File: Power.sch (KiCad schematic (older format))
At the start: 35 parts, among them T5 Test_Point, T6 Test_Point, T7 Test_Point, U4 MP4570GF, U5 AP65251, U6 AZ1117-3.3

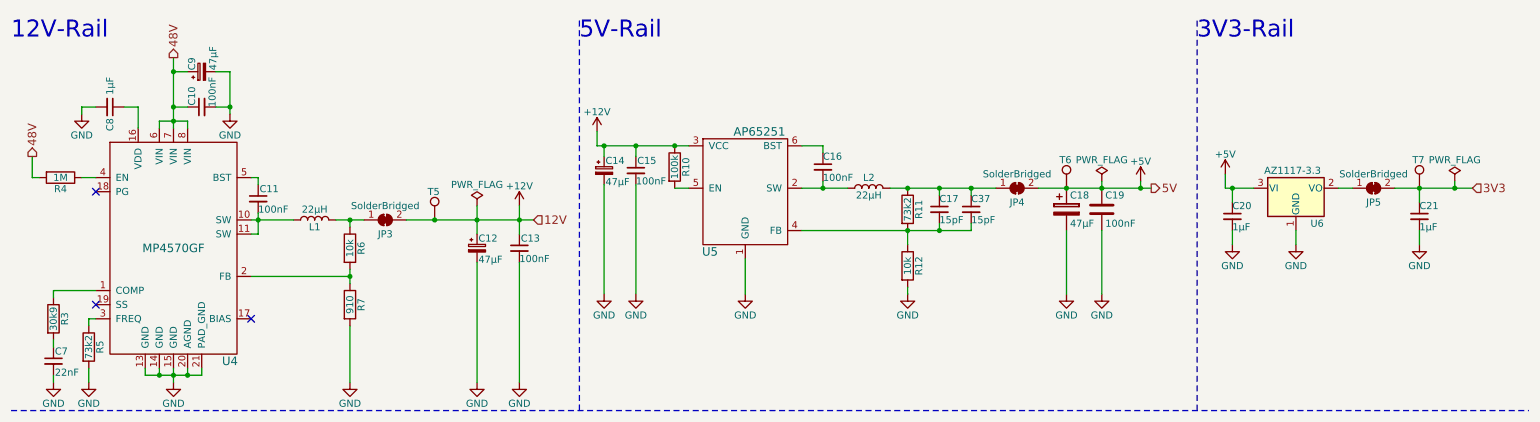
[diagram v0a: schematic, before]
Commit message: Filled in the Parts for the Fault-Indicator
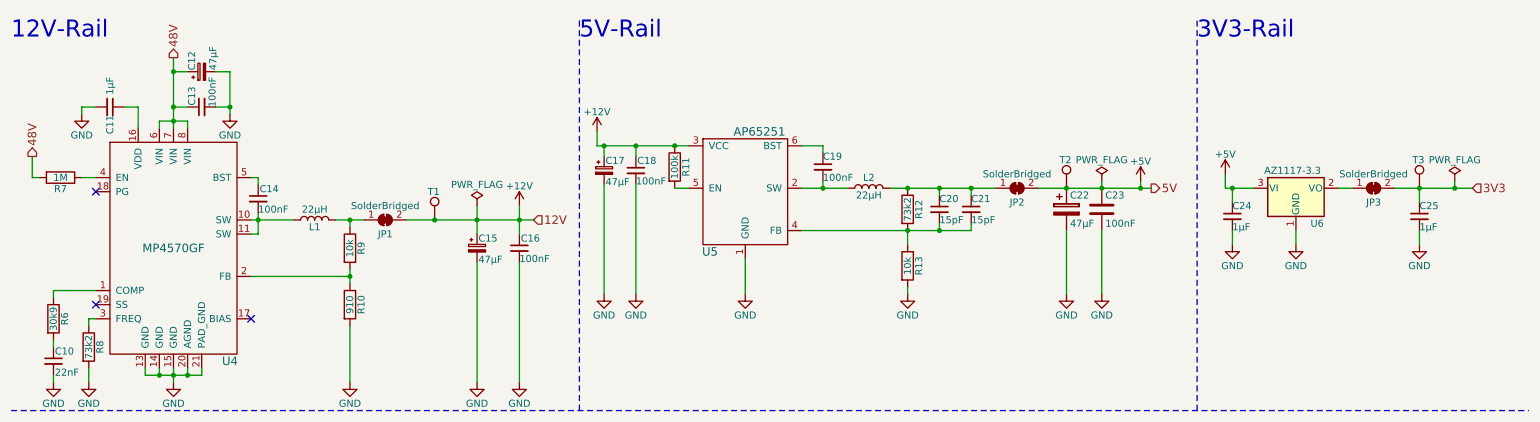
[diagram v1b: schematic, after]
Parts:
- renumbered C7 to C10, C8 to C11, C9 to C12, C10 to C13, C11 to C14, C12 to C15, C13 to C16, C14 to C17, C15 to C18, C16 to C19, C17 to C20, C37 to C21, C18 to C22, C19 to C23, C20 to C24, C21 to C25, JP3 to JP1, JP4 to JP2, JP5 to JP3, R7 to R10, R10 to R11, R11 to R12, R12 to R13, R3 to R6, R4 to R7, R5 to R8, R6 to R9, T5 to T1, T6 to T2, T7 to T3

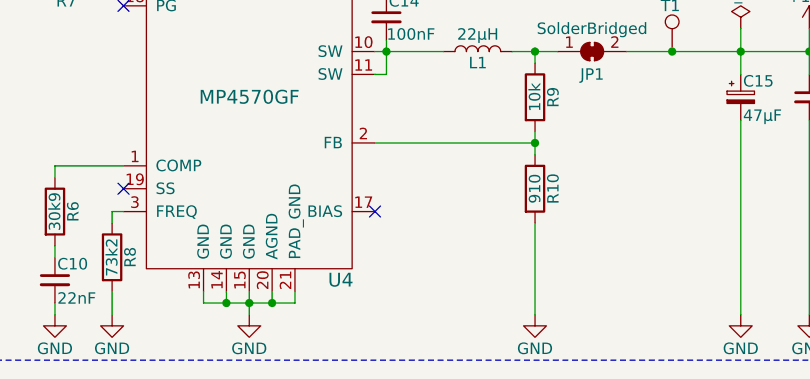
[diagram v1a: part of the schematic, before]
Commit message: Added missing bias-cap
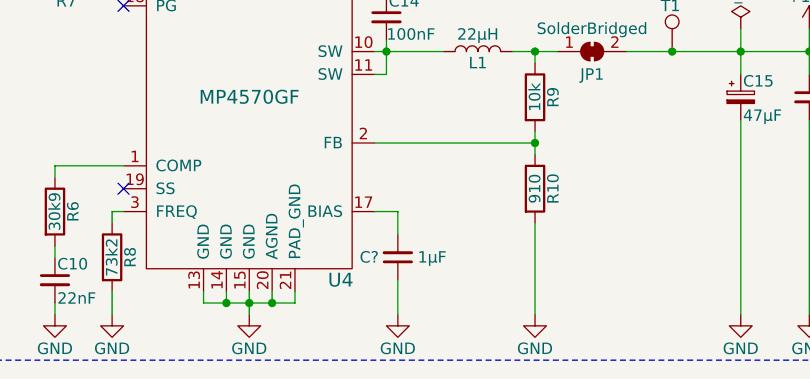
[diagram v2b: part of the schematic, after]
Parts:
- added C?: 1μF, Capacitor_SMD:C_0805_2012Metric, symbol Device:C_Small
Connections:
- net GND: now also C?.1
- net at U4.17 (BIAS): now also C?.2
- no-connect marks 3 -> 2
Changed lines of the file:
@@
 	1925 1100 2025 1100
 Connection ~ 2025 1100
-NoConn ~ 2175 2600
 $Comp
 L Device:R R9
@@
 Wire Wire Line
 	10450 1975 10450 2075
+$Comp
+L Device:C_Small C?
+U 1 1 5B7479D3
+P 2275 2800
+F 0 "C?" H 2400 2800 50  0000 C CNN
+F 1 "1μF" H 2125 2800 50  0000 C CNN
+F 2 "Capacitor_SMD:C_0805_2012Metric" H 2275 2800 50  0001 C CNN
+F 3 "~" H 2275 2800 50  0001 C CNN
+F 4 "https://www.digikey.com/product-detail/en/taiyo-yuden/TMK212B7105MG-T/587-5595-1-ND/7067270" H 2275 2800 50  0001 C CNN "Buy"
+	1    2275 2800
+	-1   0    0    1
+$EndComp
+Wire Wire Line
+	2175 2600 2275 2600
+Wire Wire Line
+	2275 2600 2275 2700
+$Comp
+L power:GND #PWR?
+U 1 1 5B74AE60
+P 2275 3050
+F 0 "#PWR?" H 2275 2800 50  0001 C CNN
+F 1 "GND" H 2275 2900 50  0000 C CNN
+F 2 "" H 2275 3050 50  0001 C CNN
+F 3 "" H 2275 3050 50  0001 C CNN
+	1    2275 3050
+	1    0    0    -1
+$EndComp
+Wire Wire Line
+	2275 2900 2275 3050
 $EndSCHEMATC

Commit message: Migrated connectors to new libraries
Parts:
- T1, T2, T3: symbol Connector_Specialized:Test_Point -> Connector:TestPoint
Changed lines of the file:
@@
 $EndComp
 $Comp
-L Connector_Specialized:Test_Point T3
+L Connector:TestPoint T3
 U 1 1 5AB61A04
 P 10450 1675
@@
 Connection ~ 10450 1675
 $Comp
-L Connector_Specialized:Test_Point T2
+L Connector:TestPoint T2
 U 1 1 5AB7C501
 P 7950 1675
@@
 Connection ~ 7950 1675
 $Comp
-L Connector_Specialized:Test_Point T1
+L Connector:TestPoint T1
 U 1 1 5AB8F83C
 P 3475 1900

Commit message: Replaced OOS-Parts
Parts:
- C11, C24, C25, C?: Buy https://www.digikey.com/product-detail/en/taiyo-yuden/TMK21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 -> https://www.digikey.com/short/jw2293
- R10: Buy https://www.digikey.com/product-detail/en/yageo/RC0603FR-07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 -> https://www.digikey.com/short/jw22zf
- R8: Buy https://www.digikey.com/product-detail/en/yageo/RC0603FR-07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 -> https://www.digikey.com/short/jw22qc
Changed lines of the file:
@@
 F 2 "Resistor_SMD:R_0603_1608Metric" V 955 2800 50  0001 C CNN
 F 3 "" H 1025 2800 50  0001 C CNN
-F 4 "https://www.digikey.com/product-detail/en/yageo/RC0603FR-0773K2L/311-73.2KHRCT-ND/730321" V 1025 2800 50  0001 C CNN "Buy"
+F 4 "https://www.digikey.com/short/jw22qc" V 1025 2800 50  0001 C CNN "Buy"
 	1    1025 2800
 	1    0    0    -1
@@
 F 2 "Resistor_SMD:R_0603_1608Metric" V 2805 2500 50  0001 C CNN
 F 3 "" H 2875 2500 50  0001 C CNN
-F 4 "https://www.digikey.com/product-detail/en/yageo/RC0603FR-07909RL/311-909HRCT-ND/730372" V 2875 2500 50  0001 C CNN "Buy"
+F 4 "https://www.digikey.com/short/jw22zf" V 2875 2500 50  0001 C CNN "Buy"
 	1    2875 2500
 	1    0    0    -1
@@
 F 2 "Capacitor_SMD:C_0805_2012Metric" H 1175 1100 50  0001 C CNN
 F 3 "~" H 1175 1100 50  0001 C CNN
-F 4 "https://www.digikey.com/product-detail/en/taiyo-yuden/TMK212B7105MG-T/587-5595-1-ND/7067270" H 1175 1100 50  0001 C CNN "Buy"
+F 4 "https://www.digikey.com/short/jw2293" H 1175 1100 50  0001 C CNN "Buy"
 	1    1175 1100
 	0    1    1    0
@@
 F 2 "Capacitor_SMD:C_0805_2012Metric" H 9163 1725 50  0001 C CNN
 F 3 "~" H 9125 1875 50  0001 C CNN
-F 4 "https://www.digikey.com/product-detail/en/taiyo-yuden/TMK212B7105MG-T/587-5595-1-ND/7067270" H 9125 1875 50  0001 C CNN "Buy"
+F 4 "https://www.digikey.com/short/jw2293" H 9125 1875 50  0001 C CNN "Buy"
 	1    9125 1875
 	1    0    0    -1
@@
 F 2 "Capacitor_SMD:C_0805_2012Metric" H 10488 1725 50  0001 C CNN
 F 3 "~" H 10450 1875 50  0001 C CNN
-F 4 "https://www.digikey.com/product-detail/en/taiyo-yuden/TMK212B7105MG-T/587-5595-1-ND/7067270" H 10450 1875 50  0001 C CNN "Buy"
+F 4 "https://www.digikey.com/short/jw2293" H 10450 1875 50  0001 C CNN "Buy"
 	1    10450 1875
 	1    0    0    -1
@@
 F 2 "Capacitor_SMD:C_0805_2012Metric" H 2275 2800 50  0001 C CNN
 F 3 "~" H 2275 2800 50  0001 C CNN
-F 4 "https://www.digikey.com/product-detail/en/taiyo-yuden/TMK212B7105MG-T/587-5595-1-ND/7067270" H 2275 2800 50  0001 C CNN "Buy"
+F 4 "https://www.digikey.com/short/jw2293" H 2275 2800 50  0001 C CNN "Buy"
 	1    2275 2800
 	-1   0    0    1

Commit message: Replaced OOS 10k-Resistor
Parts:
- R13, R9: Buy https://www.digikey.com/product-detail/en/bourns-inc/CR0603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 -> https://www.digikey.com/short/jw22d4
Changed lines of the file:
@@
 F 2 "Resistor_SMD:R_0603_1608Metric" V 6755 2225 50  0001 C CNN
 F 3 "" H 6825 2225 50  0001 C CNN
-F 4 "https://www.digikey.com/product-detail/en/bourns-inc/CR0603-FX-1002HLF/CR0603-FX-1002HLFCT-ND/3925297" V 6825 2225 50  0001 C CNN "Buy"
+F 4 "https://www.digikey.com/short/jw22d4" V 6825 2225 50  0001 C CNN "Buy"
 	1    6825 2225
 	1    0    0    -1
@@
 F 2 "Resistor_SMD:R_0603_1608Metric" V 2805 2100 50  0001 C CNN
 F 3 "" H 2875 2100 50  0001 C CNN
-F 4 "https://www.digikey.com/product-detail/en/bourns-inc/CR0603-FX-1002HLF/CR0603-FX-1002HLFCT-ND/3925297" V 2875 2100 50  0001 C CNN "Buy"
+F 4 "https://www.digikey.com/short/jw22d4" V 2875 2100 50  0001 C CNN "Buy"
 	1    2875 2100
 	1    0    0    -1

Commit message: Replaced OOS 1M-Resistor
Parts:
- R7: Buy https://www.digikey.com/product-detail/en/stackpole-electro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 -> https://www.digikey.com/short/jw2wc9
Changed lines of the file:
@@
 F 2 "Resistor_SMD:R_0603_1608Metric" V 755 1600 50  0001 C CNN
 F 3 "" H 825 1600 50  0001 C CNN
-F 4 "https://www.digikey.com/product-detail/en/stackpole-electronics-inc/RMCF0603JG1M00/RMCF0603JG1M00CT-ND/6053178" V 825 1600 50  0001 C CNN "Buy"
+F 4 "https://www.digikey.com/short/jw2wc9" V 825 1600 50  0001 C CNN "Buy"
 	1    825  1600
 	0    1    1    0

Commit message: Replaced OOS 1μF 100V Capacitor
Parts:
- C13, C14: Buy https://www.digikey.com/product-detail/en/samsung-electro-m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 -> https://www.digikey.com/short/jw2w8v
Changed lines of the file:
@@
 F 2 "Capacitor_SMD:C_0805_2012Metric" H 2225 1750 50  0001 C CNN
 F 3 "" H 2225 1750 50  0001 C CNN
-F 4 "https://www.digikey.com/product-detail/en/samsung-electro-mechanics/CL21B104KCFWPNE/1276-6733-1-ND/5961592" H 2225 1750 50  0001 C CNN "Buy"
+F 4 "https://www.digikey.com/short/jw2w8v" H 2225 1750 50  0001 C CNN "Buy"
 	1    2225 1750
 	1    0    0    -1
@@
 F 2 "Capacitor_SMD:C_0805_2012Metric" H 1825 1100 50  0001 C CNN
 F 3 "" H 1825 1100 50  0001 C CNN
-F 4 "https://www.digikey.com/product-detail/en/samsung-electro-mechanics/CL21B104KCFWPNE/1276-6733-1-ND/5961592" H 1825 1100 50  0001 C CNN "Buy"
+F 4 "https://www.digikey.com/short/jw2w8v" H 1825 1100 50  0001 C CNN "Buy"
 	1    1825 1100
 	0    -1   -1   0

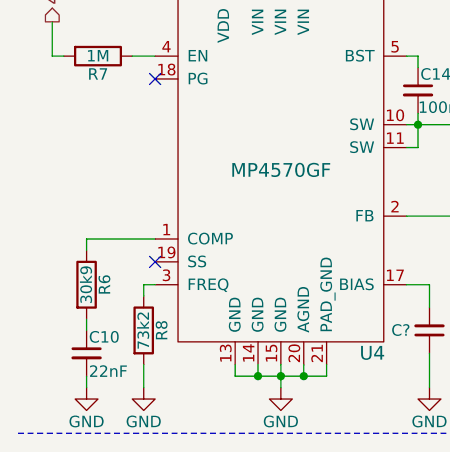
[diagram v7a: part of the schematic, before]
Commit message: Added Recalculation-Note
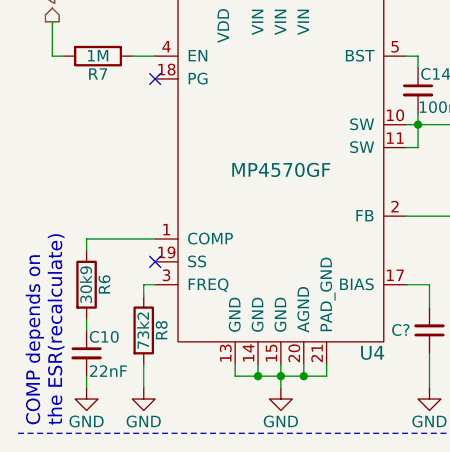
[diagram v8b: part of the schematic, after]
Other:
- note added: "COMP depends on\nthe ESR(recalculate)"
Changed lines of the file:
@@
 Wire Wire Line
 	2275 2900 2275 3050
+Text Notes 675  3225 1    60   ~ 0
+COMP depends on\nthe ESR(recalculate)
 $EndSCHEMATC
